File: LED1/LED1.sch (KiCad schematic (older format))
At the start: 13 parts, among them J1 Conn_01x02_Female, U1 AL8805

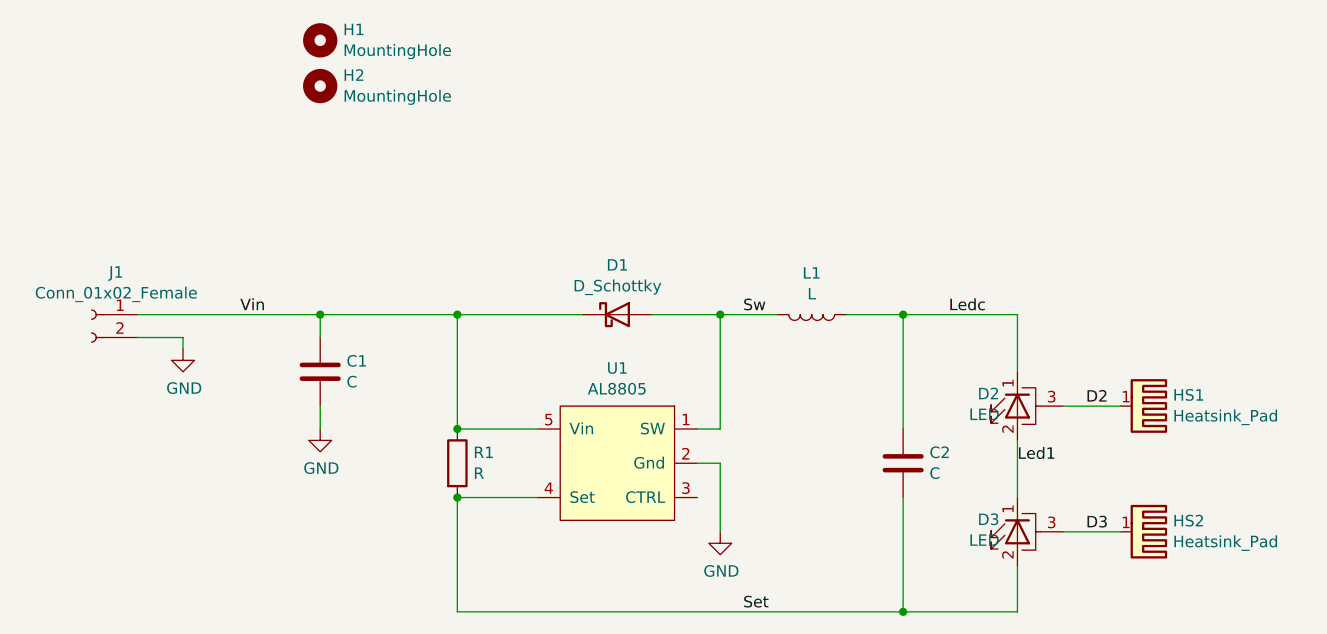
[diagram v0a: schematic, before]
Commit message: Updating component values.  Updates for new Kicad version.
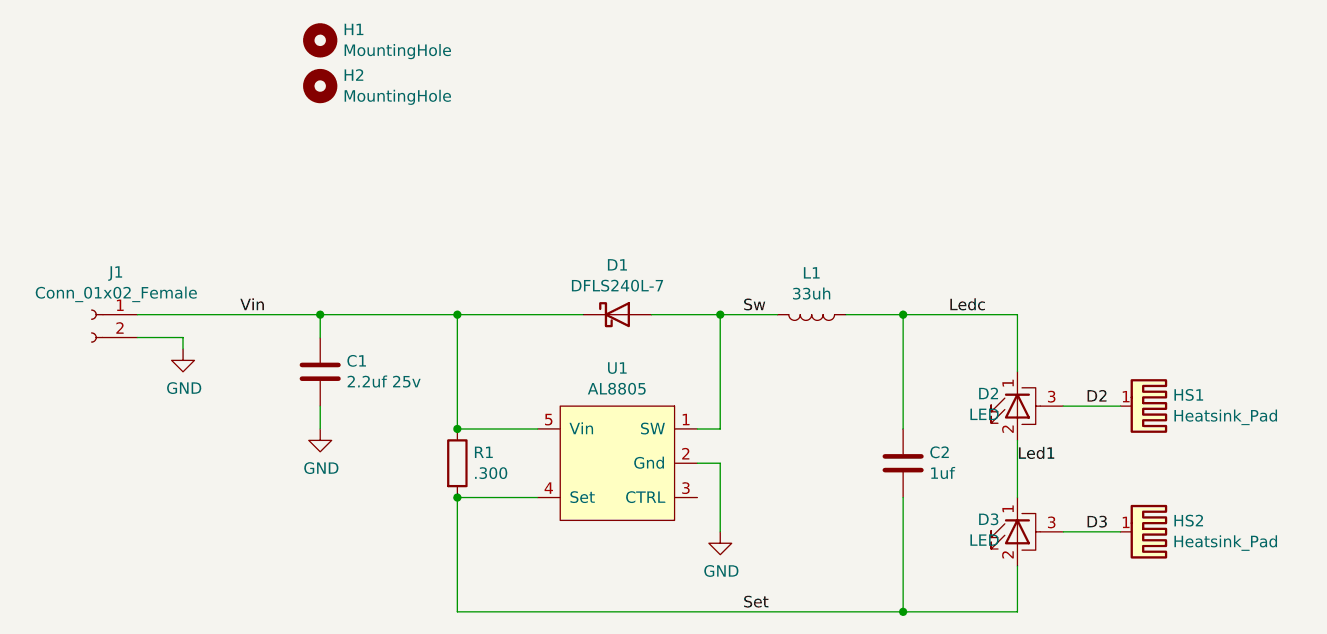
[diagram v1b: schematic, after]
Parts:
- C1: value C -> 2.2uf 25v
- C2: value C -> 1uf
- D1: value D_Schottky -> DFLS240L-7
- L1: value L -> 33uh
- R1: value R -> .300
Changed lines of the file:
@@
 P 6200 3750
 F 0 "D1" H 6200 3966 50  0000 C CNN
-F 1 "D_Schottky" H 6200 3875 50  0000 C CNN
+F 1 "DFLS240L-7" H 6200 3875 50  0000 C CNN
 F 2 "Diode_SMD:D_SOD-123" H 6200 3750 50  0001 C CNN
 F 3 "~" H 6200 3750 50  0001 C CNN
@@
 P 5500 4400
 F 0 "R1" H 5570 4446 50  0000 L CNN
-F 1 "R" H 5570 4355 50  0000 L CNN
+F 1 ".300" H 5570 4355 50  0000 L CNN
 F 2 "Resistor_SMD:R_0805_2012Metric_Pad1.15x1.40mm_HandSolder" V 5430 4400 50  0001 C CNN
 F 3 "~" H 5500 4400 50  0001 C CNN
@@
 P 4900 4000
 F 0 "C1" H 5015 4046 50  0000 L CNN
-F 1 "C" H 5015 3955 50  0000 L CNN
+F 1 "2.2uf 25v" H 5015 3955 50  0000 L CNN
 F 2 "Capacitor_SMD:C_0805_2012Metric_Pad1.15x1.40mm_HandSolder" H 4938 3850 50  0001 C CNN
 F 3 "~" H 4900 4000 50  0001 C CNN
@@
 P 7450 4400
 F 0 "C2" H 7565 4446 50  0000 L CNN
-F 1 "C" H 7565 4355 50  0000 L CNN
+F 1 "1uf" H 7565 4355 50  0000 L CNN
 F 2 "Capacitor_SMD:C_1206_3216Metric_Pad1.42x1.75mm_HandSolder" H 7488 4250 50  0001 C CNN
 F 3 "~" H 7450 4400 50  0001 C CNN
@@
 P 7050 3750
 F 0 "L1" V 6869 3750 50  0000 C CNN
-F 1 "L" V 6960 3750 50  0000 C CNN
+F 1 "33uh" V 6960 3750 50  0000 C CNN
 F 2 "0MiscParts:LPS-6235" H 7050 3750 50  0001 C CNN
 F 3 "~" H 7050 3750 50  0001 C CNN
